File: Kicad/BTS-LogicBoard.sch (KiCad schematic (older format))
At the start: 36 parts, among them J1 Conn_01x06, J2 Conn_01x04, J3 Conn_01x02, Q1 BC817, Q2 BC807, Q3 BC817, SW1 SW_DPDT_x2, SW2 SW_DPDT_x2, U1 NCS2252SN2T1G, U2 NE555D

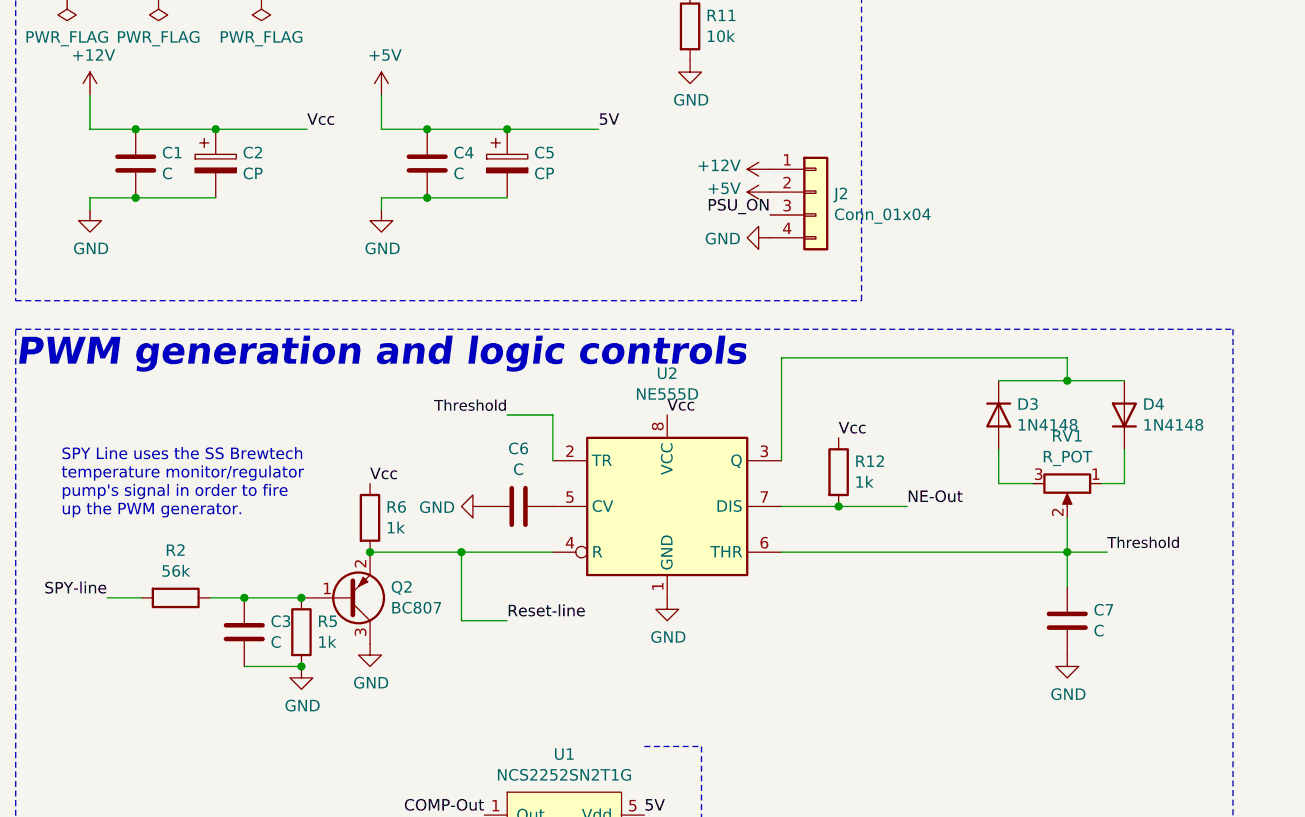
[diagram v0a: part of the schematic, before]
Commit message: Started to assign footprints
Signed-off-by: bebenlebricolo <benoittarrade@hotmail.fr>
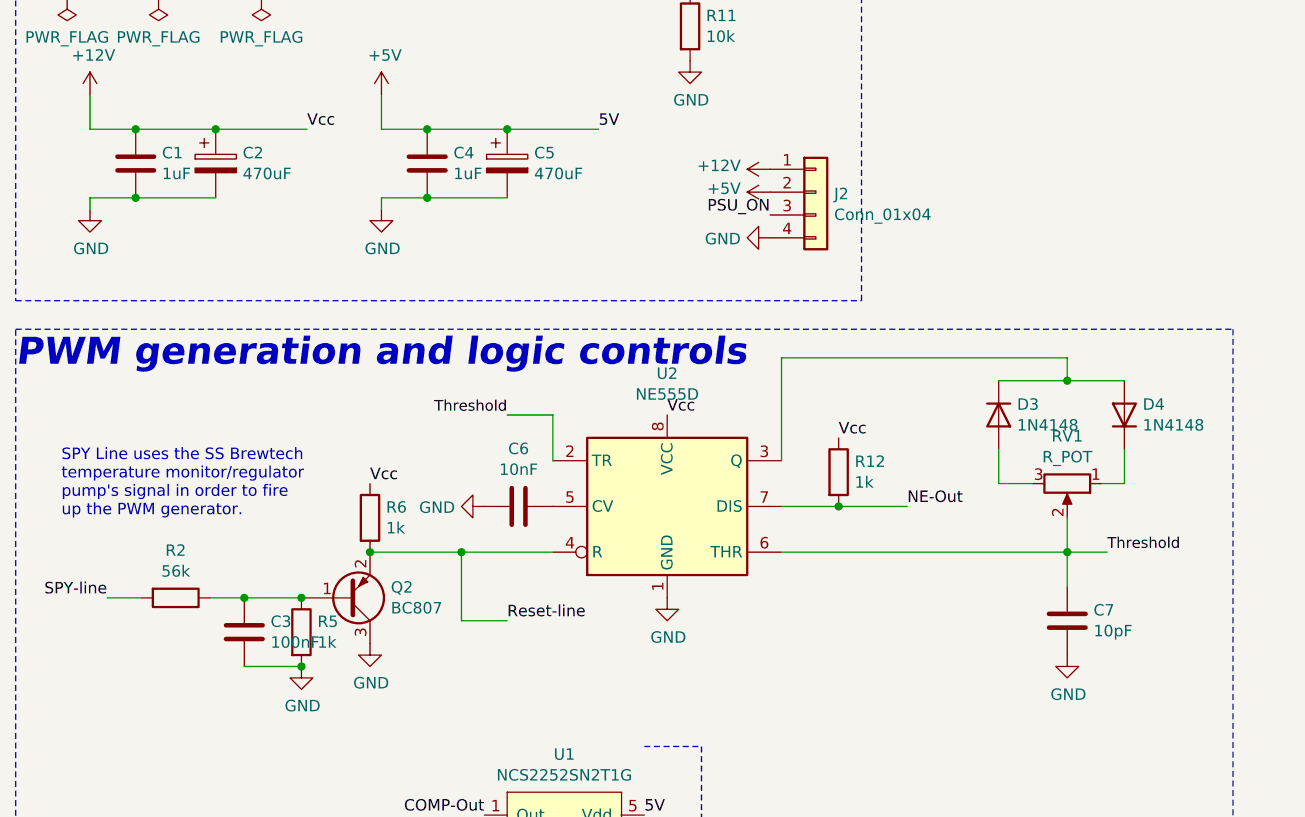
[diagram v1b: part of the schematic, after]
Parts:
- C1, C4: value C -> 1uF; footprint (none) -> Capacitor_SMD:C_1206_3216Metric_Pad1.33x1.80mm_HandSolder
- C2, C5: value CP -> 470uF; footprint (none) -> Capacitor_SMD:CP_Elec_10x10
- C3: value C -> 100nF; footprint (none) -> Capacitor_SMD:C_1206_3216Metric_Pad1.33x1.80mm_HandSolder
- C6: value C -> 10nF; footprint (none) -> Capacitor_SMD:C_1206_3216Metric_Pad1.33x1.80mm_HandSolder
- C7: value C -> 10pF; footprint (none) -> Capacitor_SMD:C_1206_3216Metric_Pad1.33x1.80mm_HandSolder
- D1, D2: footprint (none) -> LED_THT:LED_D3.0mm
- J1: footprint (none) -> BTS-LogicBoard:Molex_MicroLock_1.25_01x06
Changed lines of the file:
@@
 P 1150 1750
 F 0 "C1" H 1265 1796 50  0000 L CNN
-F 1 "C" H 1265 1705 50  0000 L CNN
-F 2 "" H 1188 1600 50  0001 C CNN
+F 1 "1uF" H 1265 1705 50  0000 L CNN
+F 2 "Capacitor_SMD:C_1206_3216Metric_Pad1.33x1.80mm_HandSolder" H 1188 1600 50  0001 C CNN
 F 3 "~" H 1150 1750 50  0001 C CNN
 	1    1150 1750
@@
 Connection ~ 5225 3450
 $Comp
-L Device:C C7
-U 1 1 613C5EC1
-P 5225 3750
-F 0 "C7" H 5340 3796 50  0000 L CNN
-F 1 "C" H 5340 3705 50  0000 L CNN
-F 2 "" H 5263 3600 50  0001 C CNN
-F 3 "~" H 5225 3750 50  0001 C CNN
-	1    5225 3750
-	1    0    0    -1
-$EndComp
-$Comp
 L power:GND #PWR0106
 U 1 1 613C656D
@@
 P 2825 3250
 F 0 "C6" V 2573 3250 50  0000 C CNN
-F 1 "C" V 2664 3250 50  0000 C CNN
-F 2 "" H 2863 3100 50  0001 C CNN
+F 1 "10nF" V 2664 3250 50  0000 C CNN
+F 2 "Capacitor_SMD:C_1206_3216Metric_Pad1.33x1.80mm_HandSolder" H 2863 3100 50  0001 C CNN
 F 3 "~" H 2825 3250 50  0001 C CNN
 	1    2825 3250
@@
 P 1625 3800
 F 0 "C3" H 1510 3754 50  0000 R CNN
-F 1 "C" H 1510 3845 50  0000 R CNN
-F 2 "" H 1663 3650 50  0001 C CNN
+F 1 "100nF" H 1510 3845 50  0000 R CNN
+F 2 "Capacitor_SMD:C_1206_3216Metric_Pad1.33x1.80mm_HandSolder" H 1663 3650 50  0001 C CNN
 F 3 "~" H 1625 3800 50  0001 C CNN
 	1    1625 3800
@@
 P 1500 1750
 F 0 "C2" H 1618 1796 50  0000 L CNN
-F 1 "CP" H 1618 1705 50  0000 L CNN
-F 2 "" H 1538 1600 50  0001 C CNN
+F 1 "470uF" H 1618 1705 50  0000 L CNN
+F 2 "Capacitor_SMD:CP_Elec_10x10" H 1538 1600 50  0001 C CNN
 F 3 "~" H 1500 1750 50  0001 C CNN
 	1    1500 1750
@@
 F 0 "D1" V 1839 6032 50  0000 R CNN
 F 1 "LED" V 1748 6032 50  0000 R CNN
-F 2 "" H 1800 6150 50  0001 C CNN
+F 2 "LED_THT:LED_D3.0mm" H 1800 6150 50  0001 C CNN
 F 3 "~" H 1800 6150 50  0001 C CNN
 	1    1800 6150
@@
 F 0 "D2" V 4014 6432 50  0000 R CNN
 F 1 "LED" V 3923 6432 50  0000 R CNN
-F 2 "" H 3975 6550 50  0001 C CNN
+F 2 "LED_THT:LED_D3.0mm" H 3975 6550 50  0001 C CNN
 F 3 "~" H 3975 6550 50  0001 C CNN
 	1    3975 6550
@@
 P 2775 1750
 F 0 "C5" H 2893 1796 50  0000 L CNN
-F 1 "CP" H 2893 1705 50  0000 L CNN
-F 2 "" H 2813 1600 50  0001 C CNN
+F 1 "470uF" H 2893 1705 50  0000 L CNN
+F 2 "Capacitor_SMD:CP_Elec_10x10" H 2813 1600 50  0001 C CNN
 F 3 "~" H 2775 1750 50  0001 C CNN
 	1    2775 1750
@@
 P 2425 1750
 F 0 "C4" H 2540 1796 50  0000 L CNN
-F 1 "C" H 2540 1705 50  0000 L CNN
-F 2 "" H 2463 1600 50  0001 C CNN
+F 1 "1uF" H 2540 1705 50  0000 L CNN
+F 2 "Capacitor_SMD:C_1206_3216Metric_Pad1.33x1.80mm_HandSolder" H 2463 1600 50  0001 C CNN
 F 3 "~" H 2425 1750 50  0001 C CNN
 	1    2425 1750
@@
 F 0 "J1" H 10655 5842 50  0000 L CNN
 F 1 "Conn_01x06" H 10655 5751 50  0000 L CNN
-F 2 "" H 10575 5850 50  0001 C CNN
+F 2 "BTS-LogicBoard:Molex_MicroLock_1.25_01x06" H 10575 5850 50  0001 C CNN
 F 3 "~" H 10575 5850 50  0001 C CNN
 	1    10575 5850
@@
 Text Notes 7300 5350 0    118  Italic 24
 Input and Output signal connections
+$Comp
+L Device:C C7
+U 1 1 613C5EC1
+P 5225 3750
+F 0 "C7" H 5340 3796 50  0000 L CNN
+F 1 "10pF" H 5340 3705 50  0000 L CNN
+F 2 "Capacitor_SMD:C_1206_3216Metric_Pad1.33x1.80mm_HandSolder" H 5263 3600 50  0001 C CNN
+F 3 "~" H 5225 3750 50  0001 C CNN
+	1    5225 3750
+	1    0    0    -1
+$EndComp
 $EndSCHEMATC

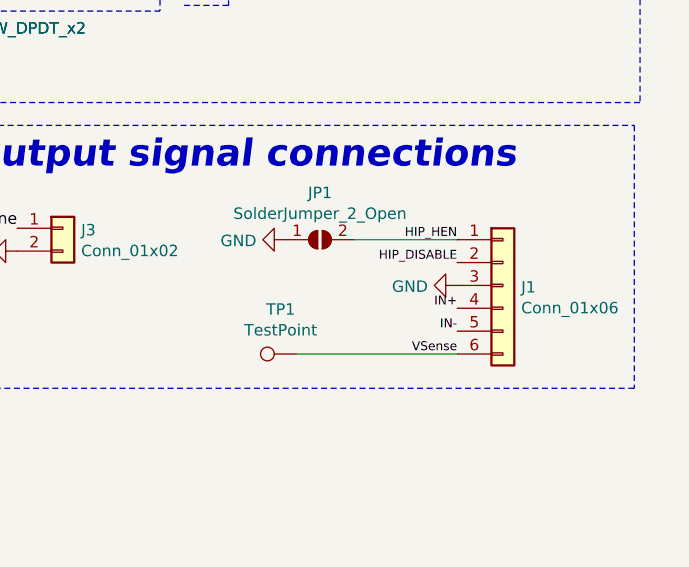
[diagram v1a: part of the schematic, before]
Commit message: Added fan triggering simulation
Signed-off-by: bebenlebricolo <benoittarrade@hotmail.fr>
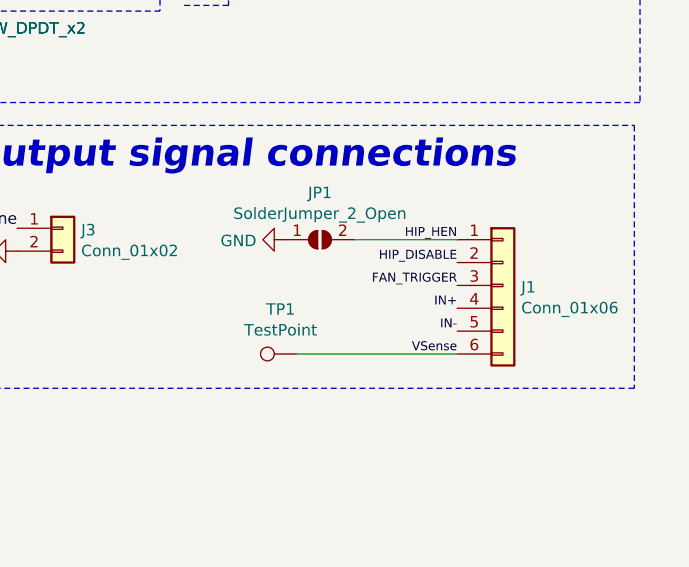
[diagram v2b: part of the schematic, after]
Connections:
- net GND: no longer J1.3 (Pin_3)
- new net FAN_TRIGGER: J1.3 (Pin_3)
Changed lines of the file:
@@
 Text Label 10375 5750 2    39   ~ 0
 HIP_DISABLE
-$Comp
-L power:GND #PWR0121
-U 1 1 615EE7D8
-P 10375 5850
-F 0 "#PWR0121" H 10375 5600 50  0001 C CNN
-F 1 "GND" V 10380 5722 50  0000 R CNN
-F 2 "" H 10375 5850 50  0001 C CNN
-F 3 "" H 10375 5850 50  0001 C CNN
-	1    10375 5850
-	0    1    1    0
-$EndComp
 Text Label 10375 5950 2    39   ~ 0
 IN+
@@
 	1    0    0    -1
 $EndComp
+Text Label 10375 5850 2    39   ~ 0
+FAN_TRIGGER
 $EndSCHEMATC
